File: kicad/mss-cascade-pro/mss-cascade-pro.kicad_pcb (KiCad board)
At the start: 2 copper layers, 127 x 76.2 mm, 161 parts, among them J1 Molex 0532610471, J10 Screw_Terminal_01x02, J11 Molex 0532610471, J12 Molex 0532610471, J13 8P8C, J14 SM04B-SRSS, J15 SM04B-SRSS, J16 SM04B-SRSS, J17 SM04B-SRSS, J18 AVR-ISP, J19 Screw_Terminal_01x02, J2 Molex 0532610471, J3 Screw_Terminal_01x02, J4 8P8C, J5 Screw_Terminal_01x02, J6 Screw_Terminal_01x02, J7 Screw_Terminal_01x02, J8 8P8C, J9 Screw_Terminal_01x02, K1 AGQ200A4H, K2 AGQ200A4H, K3 AGQ200A4H, Q1 ZXMS6004FF, Q2 DRDC3105-7, SW1 JS202011SCQN, SW2 JS202011SCQN, U1 AP63205WU, U2 AP3012, U3 74HC4049, U4 74HC4049, U5 PCA9555PW, U6 ATtiny861A-S

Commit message: Continued work on cascade pro
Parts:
- removed C2, C21: 0.1uF, Capacitor_SMD:C_0805_2012Metric
- removed C20, C3: 10uF, Capacitor_SMD:C_0805_2012Metric
- removed C5: 22uF, Capacitor_SMD:C_0805_2012Metric
- removed D13, D14, D15, D16, D6: CDBM140G, ISE_Generic:SOD-123T
- removed D3: SMAJ18A-TP, Diode_SMD:D_SMA
- removed J14: SM04B-SRSS, Connector_JST:JST_SH_SM04B-SRSS-TB_1x04-1MP_P1.00mm_Horizontal
- removed J19: Screw_Terminal_01x02, TerminalBlock_MetzConnect:TerminalBlock_MetzConnect_Type059_RT06303HBWC_1x03_P3.50mm_Horizontal
- removed J4: 8P8C, Connector_RJ:RJ45_Amphenol_54602-x08_Horizontal
- removed JP14, JP15, JP21, JP5: SolderJumper_2_Bridged, Jumper:SolderJumper-2_P1.3mm_Bridged_RoundedPad1.0x1.5mm
- removed JP16, JP17, JP18, JP19, JP20: SolderJumper_2_Open, Jumper:SolderJumper-2_P1.3mm_Open_RoundedPad1.0x1.5mm
- removed K1, K2, K3: AGQ200A4H, ISE_UltraLibrarian:RELAY_AGQ_A_PAN
- removed L1: 4.7uH, ISE_UltraLibrarian:MSS6132-xxxMLC
- removed Q1: ZXMS6004FF, Package_TO_SOT_SMD:SOT-23
- removed Q2: DRDC3105-7, Package_TO_SOT_SMD:SOT-23
- removed R2: 1k, Resistor_SMD:R_0805_2012Metric
- removed R41, R42: 10k, Resistor_SMD:R_0805_2012Metric
- removed TP17, TP18, TP19, TP20, TP21, TP22, TP23: TestPoint, TestPoint:TestPoint_Pad_D2.0mm
- added SW3: SW_DIP_x08, Button_Switch_SMD:SW_DIP_SPSTx08_Slide_6.7x21.88mm_W8.61mm_P2.54mm_LowProfile, F.Cu at (84.6, 183.4)
- R1: value 1k -> 10k
- U1: value AP63205WU -> AP7381-50Y; footprint Package_TO_SOT_SMD:TSOT-23-6 -> ISE_Generic:SOT-89-3
- moved R1 37.6 mm to (85.1, 136.0)
- moved R28 23.4 mm to (124.6, 149.0)
- moved R29 18.4 mm to (124.9, 152.4)
- moved D11 17.5 mm to (141.6, 162.7)
- moved C4 8.57 mm to (54.7, 161.4), turned to 0 degrees
- moved D12 6.15 mm to (141.6, 144.0)
- moved J15 6.14 mm to (149.0, 153.5)
- moved J16 6.14 mm to (149.0, 164.1)
- moved J17 6.14 mm to (149.0, 142.9)
- moved U1 4.46 mm to (55.5, 166.0), turned to 0 degrees
- moved C1 1.02 mm to (58.4, 175.0), turned to 0 degrees
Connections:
- net /B_SIGNAL_G renamed /B_U_SIGNAL_G
- net /B_SIGNAL_R renamed /B_U_SIGNAL_R
- net /B_SIGNAL_Y renamed /B_U_SIGNAL_Y
- net /C_SIGNAL_G renamed /B_L_SIGNAL_G
- net /C_SIGNAL_R renamed /B_L_SIGNAL_R
- net /C_SIGNAL_Y renamed /B_L_SIGNAL_Y
- net /MAIN_AA_IN renamed /B_ADV_APPROACH
- net /POINTS_AA_IN renamed /A_ADV_APPROACH
- net Net-(R39-Pad1) renamed /TEST_MODE
- C1 pad 1: Net-(C1-Pad1) -> /VPWR
- D1 pad 1: Net-(C1-Pad1) -> /VPWR
- D10 pad 1: /POINTS_S -> /A_ADJACENT
- D11 pad 2: /POINTS_A_OUT -> /B_ADJACENT
- D12 pad 2: /POINTS_S -> /A_ADJACENT
- D2 pad 1: Net-(C1-Pad1) -> /VPWR
- D7 pad 1: /MAIN_S -> /B_ADJACENT
- J13 pad 2: /POINTS_A_IN -> /A_APPROACH
- J13 pad 3: /POINTS_AA_OUT -> /B_APPROACH
- J13 pad 4: /POINTS_S -> /A_ADJACENT
- J13 pad 6: /POINTS_A_OUT -> /B_ADJACENT
- J13 pad 8: /POINTS_DA_OUT -> /A_DIV_APRCH
- J15 pad 2: +5V -> /VPWR
- J16 pad 2: +5V -> /VPWR
- J16 pad 3: /MAIN_S -> /B_ADJACENT
- J17 pad 2: +5V -> /VPWR
- J17 pad 3: /POINTS_S -> /A_ADJACENT
- J8 pad 2: /MAIN_A_IN -> /B_APPROACH
- J8 pad 3: /MAIN_AA_OUT -> /A_APPROACH
- J8 pad 4: /MAIN_S -> /B_ADJACENT
- J8 pad 6: /MAIN_A_OUT -> /A_ADJACENT
- J8 pad 7: Net-(J8-Pad7) -> Net-(J13-Pad7)
- J8 pad 8: unconnected-(J8-Pad8) -> /B_DIV_APRCH
- R1 pad 1: Net-(R1-Pad1) -> Net-(U3-Pad5)
- R1 pad 2: +12V -> Net-(R28-Pad1)
- R22 pad 2: /POINTS_S -> /A_ADJACENT
- R23 pad 2: /POINTS_A_OUT -> /B_ADJACENT
- R24 pad 2: /POINTS_AA_OUT -> /B_APPROACH
- R26 pad 1: /POINTS_A_IN -> /A_APPROACH
- R28 pad 1: +12V -> Net-(R28-Pad1)
- R28 pad 2: /SIDE_AA_IN -> /A_DIV_APRCH
- R29 pad 1: +12V -> Net-(R28-Pad1)
- R29 pad 2: Net-(JP21-Pad1) -> /B_DIV_APRCH
- R30 pad 1: /POINTS_S -> /A_ADJACENT
- R31 pad 1: /POINTS_A_OUT -> /B_ADJACENT
- R32 pad 1: /POINTS_AA_OUT -> /B_APPROACH
- R33 pad 1: /POINTS_A_IN -> /A_APPROACH
- R36 pad 1: /SIDE_AA_IN -> /A_DIV_APRCH
- R38 pad 1: /TO_NORMAL -> /B_DIV_APRCH
- SW1 pad 1: Net-(R2-Pad1) -> GND
- SW1 pad 2: Net-(K1-Pad4) -> Net-(R28-Pad1)
- SW1 pad 3: GND -> +12V
- SW1 pad 4: Net-(R2-Pad1) -> GND
- SW1 pad 5: Net-(K1-Pad4) -> Net-(R28-Pad1)
- SW1 pad 6: GND -> +12V
- U1 pad 2: Net-(C1-Pad1) -> GND
- U1 pad 3: Net-(C1-Pad1) -> /VPWR
- U3 pad 4: unconnected-(U3-Pad4) -> /MSS_V2
- U3 pad 5: GND -> Net-(U3-Pad5)
- U4 pad 4: /APPR_LT -> (no net)
- U4 pad 5: Net-(C21-Pad1) -> (no net)
- U5 pad 10: /FORCE_POINTS_AA -> /OPTION_F
- U5 pad 11: /RELAY_DRV -> /OPTION_G
- U5 pad 4: /APPR_LT -> /MSS_V2
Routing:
- net +5V: track 432.7 -> 183.1 mm, vias 4 -> 0
- net /VPWR: track 0.00 -> 176.1 mm
- net /A_ADJACENT: track 0.00 -> 130.2 mm, vias 0 -> 4
- net /B_ADJACENT: track 0.00 -> 123.8 mm, vias 0 -> 4
- net /SIDE_S: track 123.5 -> 0.00 mm, vias 2 -> 0
- net /POINTS_S: track 118.9 -> 0.00 mm, vias 4 -> 0
- net /MAIN_S: track 96.7 -> 0.00 mm, vias 2 -> 0
- net /POINTS_AA_OUT: track 91.1 -> 0.00 mm, vias 6 -> 0
- net /A_APPROACH: track 0.00 -> 85.5 mm, vias 0 -> 6
- net /B_APPROACH: track 0.00 -> 81.9 mm, vias 0 -> 6
- net /POINTS_A_OUT: track 79.5 -> 0.00 mm, vias 4 -> 0
- net /SIDE_AA_IN: track 60.9 -> 0.00 mm, vias 4 -> 0
- net /POINTS_A_IN: track 56.9 -> 0.00 mm, vias 3 -> 0
- net /SIDE_A_IN: track 53.2 -> 0.00 mm, vias 2 -> 0
- net /RELAY_DRV: track 52.8 -> 0.00 mm
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- added copper zone on F.Cu, net /VPWR
- removed copper zone on F.Cu, net +5V
- removed copper zone on F.Cu, net Net-(C1-Pad1)
- removed copper zone on F.Cu, net Net-(R2-Pad1)
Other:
- board text added: "MSS-CASCADE-PRO v1.0 www.iascaled.com ©2024 Iowa Scaled Engineering"
- board text added: "SIGNAL B LOWER"
- board text added: "SIGNAL B UPPER"
- board text removed: "+5V"
- board text removed: "AL"
- board text removed: "AU"
- board text removed: "BD1 C"
- board text removed: "CONFIG SOLDER JUMPERS"
- board text removed: "Cut JP14 to disconnect MSS Port B Pin 7 from ground"
- board text removed: "Cut JP15 to disconnect MSS Port A Pin 7 from ground"
- board text removed: "Cut JP5 to disconnect MSS Port C Pin 7 from ground"
- board text removed: "GND"
- board text removed: "IN"
- board text removed: "MSS-SWITCH v1.1 www.iascaled.com ©2024 Iowa Scaled Engineering"
- board text removed: "SIGNAL C"
- board text removed: "TURNOUT"
- board text removed: "TURNOUT DIVERGING IN=GND"

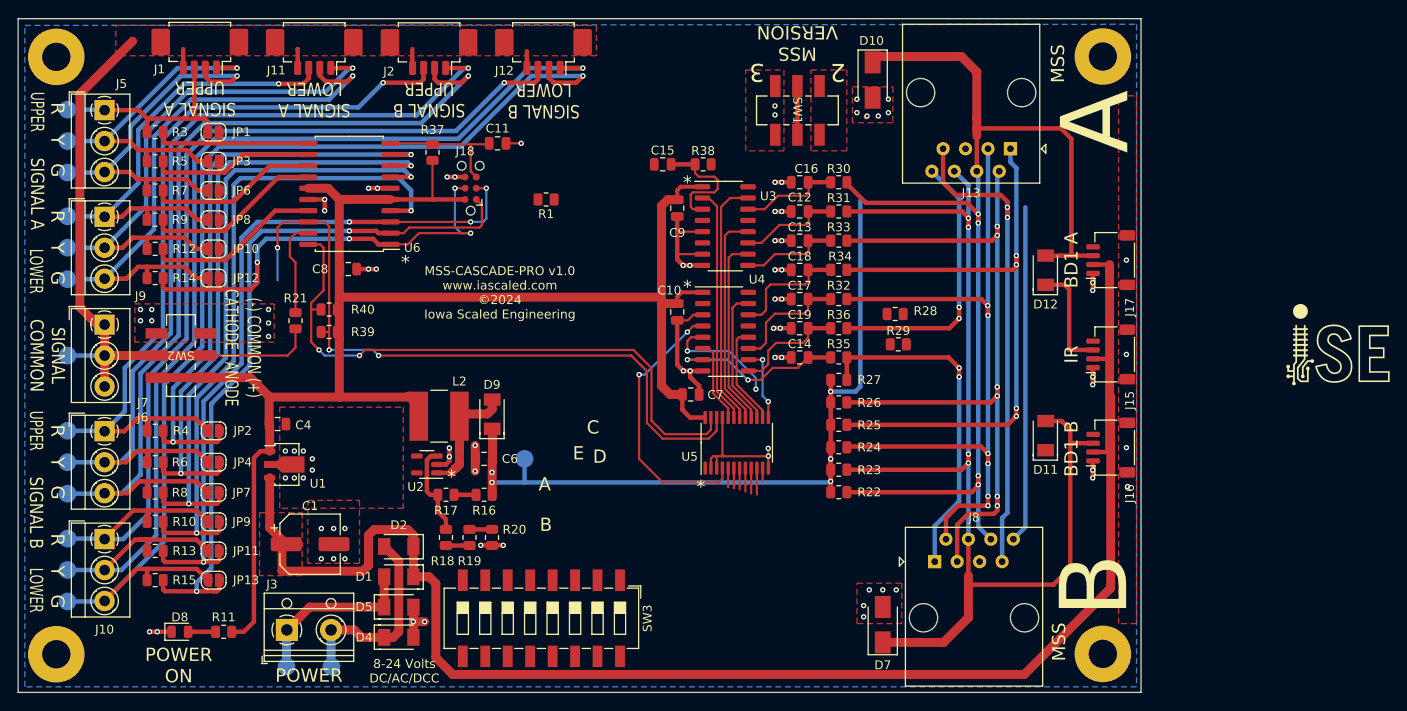
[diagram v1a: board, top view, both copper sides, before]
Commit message: Initial cut of the cascade pro idea
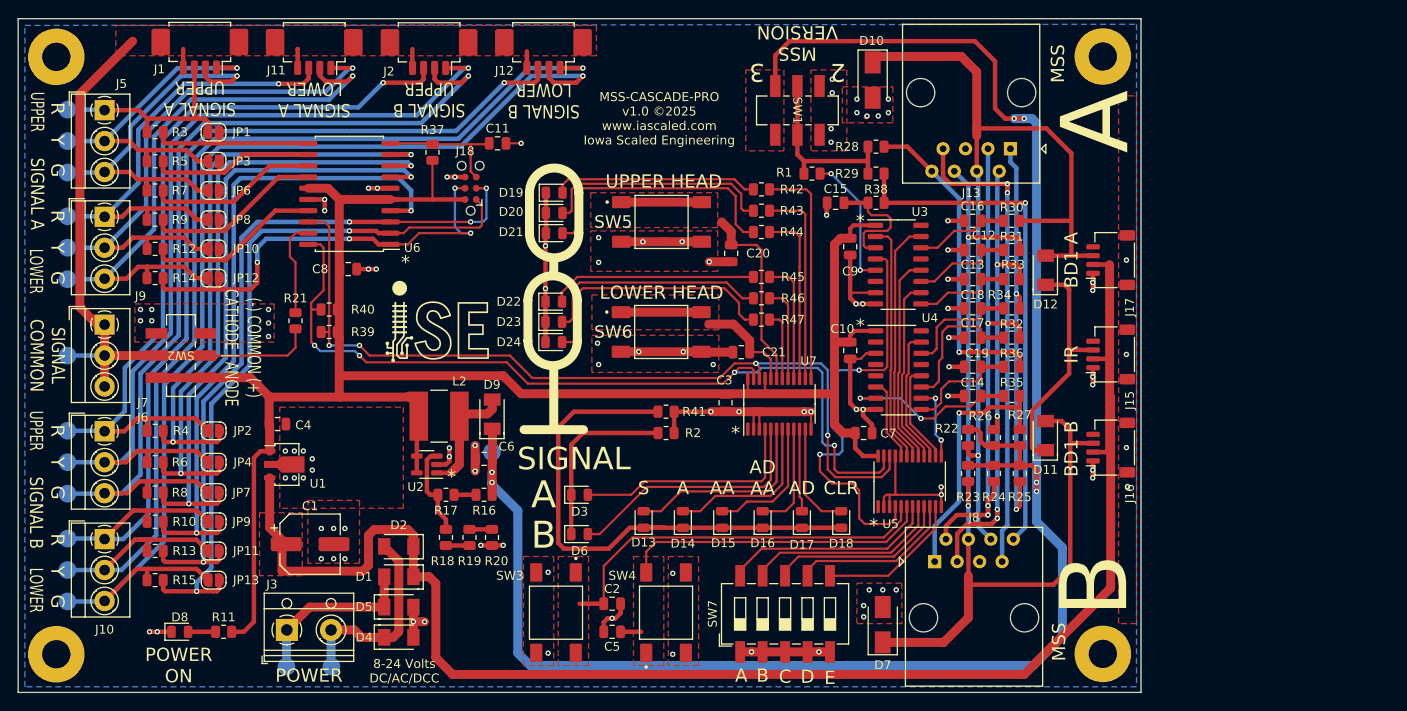
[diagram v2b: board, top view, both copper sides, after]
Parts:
- added C2: 0.1uF, Capacitor_SMD:C_0805_2012Metric, F.Cu at (92.6, 181.7)
- added C20: 0.1uF, Capacitor_SMD:C_0805_2012Metric, F.Cu at (106.0, 142.1)
- added C21: 0.1uF, Capacitor_SMD:C_0805_2012Metric, F.Cu at (107.2, 153.3)
- added C3: 0.1uF, Capacitor_SMD:C_0805_2012Metric, F.Cu at (105.4, 159.0)
- added C5: 0.1uF, Capacitor_SMD:C_0805_2012Metric, F.Cu at (92.6, 184.9)
- added D13: AMBER LED, LED_SMD:LED_0805_2012Metric, F.Cu at (96.1, 172.2)
- added D14: AMBER LED, LED_SMD:LED_0805_2012Metric, F.Cu at (100.6, 172.2)
- added D15: AMBER LED, LED_SMD:LED_0805_2012Metric, F.Cu at (105.0, 172.2)
- added D16: AMBER LED, LED_SMD:LED_0805_2012Metric, F.Cu at (109.6, 172.2)
- added D17: AMBER LED, LED_SMD:LED_0805_2012Metric, F.Cu at (114.0, 172.2)
- added D18: AMBER LED, LED_SMD:LED_0805_2012Metric, F.Cu at (118.5, 172.2)
- added D19: GREEN LED, LED_SMD:LED_0805_2012Metric, F.Cu at (86.0, 135.3)
- added D20: AMBER LED, LED_SMD:LED_0805_2012Metric, F.Cu at (86.0, 137.5)
- added D21: RED LED, LED_SMD:LED_0805_2012Metric, F.Cu at (86.0, 139.8)
- added D22: GREEN LED, LED_SMD:LED_0805_2012Metric, F.Cu at (86.0, 147.6)
- added D23: AMBER LED, LED_SMD:LED_0805_2012Metric, F.Cu at (86.0, 149.9)
- added D24: RED LED, LED_SMD:LED_0805_2012Metric, F.Cu at (86.0, 152.1)
- added D3: BLUE LED, LED_SMD:LED_0805_2012Metric, F.Cu at (88.9, 169.4)
- added D6: BLUE LED, LED_SMD:LED_0805_2012Metric, F.Cu at (88.9, 173.9)
- added R2: 1k, Resistor_SMD:R_0805_2012Metric, F.Cu at (98.7, 162.4)
- added R41: 1k, Resistor_SMD:R_0805_2012Metric, F.Cu at (98.7, 160.0)
- added R42: 1k, Resistor_SMD:R_0805_2012Metric, F.Cu at (109.5, 134.9)
- added R43: 1k, Resistor_SMD:R_0805_2012Metric, F.Cu at (109.5, 137.3)
- added R44: 1k, Resistor_SMD:R_0805_2012Metric, F.Cu at (109.5, 139.7)
- added R45: 1k, Resistor_SMD:R_0805_2012Metric, F.Cu at (109.5, 144.8)
- added R46: 1k, Resistor_SMD:R_0805_2012Metric, F.Cu at (109.5, 147.2)
- added R47: 1k, Resistor_SMD:R_0805_2012Metric, F.Cu at (109.5, 149.6)
- added SW4: FSM4JSMATR, ISE_Generic:TE_FSM4JSMA, F.Cu at (98.7, 182.8)
- added SW5: FSM4JSMATR, ISE_Generic:TE_FSM4JSMA, F.Cu at (98.2, 138.6)
- added SW6: FSM4JSMATR, ISE_Generic:TE_FSM4JSMA, F.Cu at (98.1, 151.0)
- added SW7: SW_DIP_x05, Button_Switch_SMD:SW_DIP_SPSTx05_Slide_6.7x14.26mm_W8.61mm_P2.54mm_LowProfile, F.Cu at (112.1, 182.9)
- added U7: PCA9555PW, Package_SO:TSSOP-24_4.4x7.8mm_P0.65mm, F.Cu at (111.5, 159.1)
- SW3: value SW_DIP_x08 -> FSM4JSMATR; footprint Button_Switch_SMD:SW_DIP_SPSTx08_Slide_6.7x21.88mm_W8.61mm_P2.54mm_LowProfile -> ISE_Generic:TE_FSM4JSMA
- moved R1 30.2 mm to (115.2, 133.1)
- moved R27 21.5 mm to (138.7, 162.9), turned to 90 degrees
- moved R25 21.2 mm to (138.7, 167.0), turned to -90 degrees
- moved R34 20.0 mm to (137.8, 148.3)
- moved U3 20.0 mm to (124.9, 143.4)
- moved C10 20.0 mm to (119.5, 153.1)
- moved C7 20.0 mm to (121.0, 162.4)
- moved C9 20.0 mm to (119.5, 141.4)
- moved R30 20.0 mm to (137.8, 138.4)
- moved R31 20.0 mm to (137.8, 141.7)
- moved R32 20.0 mm to (137.8, 151.6)
- moved R33 20.0 mm to (137.8, 145.0)
- moved R35 20.0 mm to (137.8, 158.2)
- moved R36 20.0 mm to (137.8, 154.9)
- moved U4 20.0 mm to (125.0, 155.3)
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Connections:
- net Net-(R40-Pad1) renamed /SDA
- R39 pad 1: /TEST_MODE -> /SCL
- SW3 pad 1: /TEST_MODE -> /SW_A
- SW3 pad 2: /OPTION_G -> /SW_A
- SW3 pad 3: /OPTION_F -> GND
- SW3 pad 4: /OPTION_E -> GND
- U5 pad 10: /OPTION_F -> /OPTION_D
- U5 pad 11: /OPTION_G -> /OPTION_E
- U5 pad 22: /TEST_MODE -> /SCL
- U5 pad 5: /OPTION_A -> /SW_A
- U5 pad 6: /OPTION_B -> /SW_B
- U5 pad 7: /OPTION_C -> /OPTION_A
- U5 pad 8: /OPTION_D -> /OPTION_B
- U5 pad 9: /OPTION_E -> /OPTION_C
- U6 pad 18: /TEST_MODE -> /SCL
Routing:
- net +12V: track 89.6 -> 215.8 mm, vias 5 -> 6
- net /SCL: track 0.00 -> 98.2 mm, vias 0 -> 4
- net /TEST_MODE: track 80.4 -> 0.00 mm, vias 3 -> 0
- net GND: track 89.3 -> 167.2 mm, vias 83 -> 102
- net Net-(D13-Pad1): track 0.00 -> 60.7 mm
- net /SW_A: track 0.00 -> 44.3 mm
- net /SW_B: track 0.00 -> 37.3 mm
- net /A_APPROACH: track 85.5 -> 54.4 mm, vias 6 -> 4
- net Net-(U7-Pad19): track 0.00 -> 31.1 mm
- net +5V: track 183.1 -> 213.5 mm
- net Net-(D21-Pad2): track 0.00 -> 29.9 mm
- net Net-(D24-Pad2): track 0.00 -> 29.3 mm
- net Net-(D6-Pad2): track 0.00 -> 29.0 mm
- net /SDA: track 69.4 -> 97.8 mm, vias 2 -> 4
- net /A_ADJACENT: track 130.2 -> 102.8 mm, vias 4 -> 1
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- added copper zone on F.Cu, net +12V
- added copper zone on F.Cu, net /SW_A
- added copper zone on F.Cu, net /SW_B
- added copper zone on F.Cu, net Net-(U7-Pad19)
- added copper zone on F.Cu, net Net-(U7-Pad20)
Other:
- board text added: "AA"
- board text added: "AD"
- board text added: "AD AA"
- board text added: "CLR"
- board text added: "LOWER HEAD"
- board text added: "MSS-CASCADE-PRO v1.0 ©2025 www.iascaled.com Iowa Scaled Engineering"
- board text added: "S"
- board text added: "SIGNAL"
- board text added: "UPPER HEAD"
- board text removed: "Cut JP21 to disable +12V pull-up on turnout IN line"
- board text removed: "MSS-CASCADE-PRO v1.0 www.iascaled.com ©2024 Iowa Scaled Engineering"

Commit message: PCB Cleanup
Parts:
- moved C21 1.53 mm to (106.0, 152.3), turned to -90 degrees
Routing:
- net Net-(C20-Pad1): track 31.1 -> 35.4 mm
- net Net-(C21-Pad1): track 20.7 -> 21.8 mm
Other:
- board text added: "MSS-CASCADE-ADV v1.0 ©2025 www.iascaled.com Iowa Scaled Engineering"
- board text removed: "MSS-CASCADE-PRO v1.0 ©2025 www.iascaled.com Iowa Scaled Engineering"
